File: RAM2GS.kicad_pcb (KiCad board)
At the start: 4 copper layers, 67.1 x 48.5 mm, 54 parts, among them J1 Memory Expansion, J2 JTAG, U1 EPM240T100, U10 74LVC1G04GW, U2 W9864G6KH-6, U3 60M, U4 74AHCT245, U5 74AHC245, U6 74LVT245, U7 74LVT245, U8 LD1117S33, U9 74LVC1G04GW

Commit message: Documentation update
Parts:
- RN2, RN3, RN4, RN5: value 4x47 -> 4x30
- U10, U9: value 74LVC1G04GW -> 74LVC1G04
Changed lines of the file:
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@@
   )
   (page A4)
+  (title_block
+    (title "GW4203D (RAM2GS II)")
+    (date 2020-08-02)
+    (rev 1.0)
+    (company "Garrett's Workshop")
+  )
   (layers
     (0 F.Cu signal)
@@
       (effects (font (size 0.254 0.254) (thickness 0.0635)))
     )
-    (fp_text value 74LVC1G04GW (at 0.35 0 90) (layer F.Fab)
+    (fp_text value 74LVC1G04 (at 0.35 0 90) (layer F.Fab)
       (effects (font (size 0.1905 0.1905) (thickness 0.047625)))
     )
@@
       (effects (font (size 0.254 0.254) (thickness 0.0635)))
     )
-    (fp_text value 74LVC1G04GW (at 0.35 0 90) (layer F.Fab)
+    (fp_text value 74LVC1G04 (at 0.35 0 90) (layer F.Fab)
       (effects (font (size 0.1905 0.1905) (thickness 0.047625)))
     )
@@
       (effects (font (size 0.254 0.254) (thickness 0.0635)))
     )
-    (fp_text value 4x47 (at 0.3 0 90) (layer F.Fab)
+    (fp_text value 4x30 (at 0.3 0 90) (layer F.Fab)
       (effects (font (size 0.1905 0.1905) (thickness 0.047625)))
     )
@@
       (effects (font (size 0.254 0.254) (thickness 0.0635)))
     )
-    (fp_text value 4x47 (at 0.3 0 90) (layer F.Fab)
+    (fp_text value 4x30 (at 0.3 0 90) (layer F.Fab)
       (effects (font (size 0.1905 0.1905) (thickness 0.047625)))
     )
@@
       (effects (font (size 0.254 0.254) (thickness 0.0635)))
     )
-    (fp_text value 4x47 (at 0.3 0) (layer F.Fab)
+    (fp_text value 4x30 (at 0.3 0) (layer F.Fab)
       (effects (font (size 0.1905 0.1905) (thickness 0.047625)))
     )
@@
       (effects (font (size 0.254 0.254) (thickness 0.0635)))
     )
-    (fp_text value 4x47 (at 0.3 0) (layer F.Fab)
+    (fp_text value 4x30 (at 0.3 0) (layer F.Fab)
       (effects (font (size 0.1905 0.1905) (thickness 0.047625)))
     )

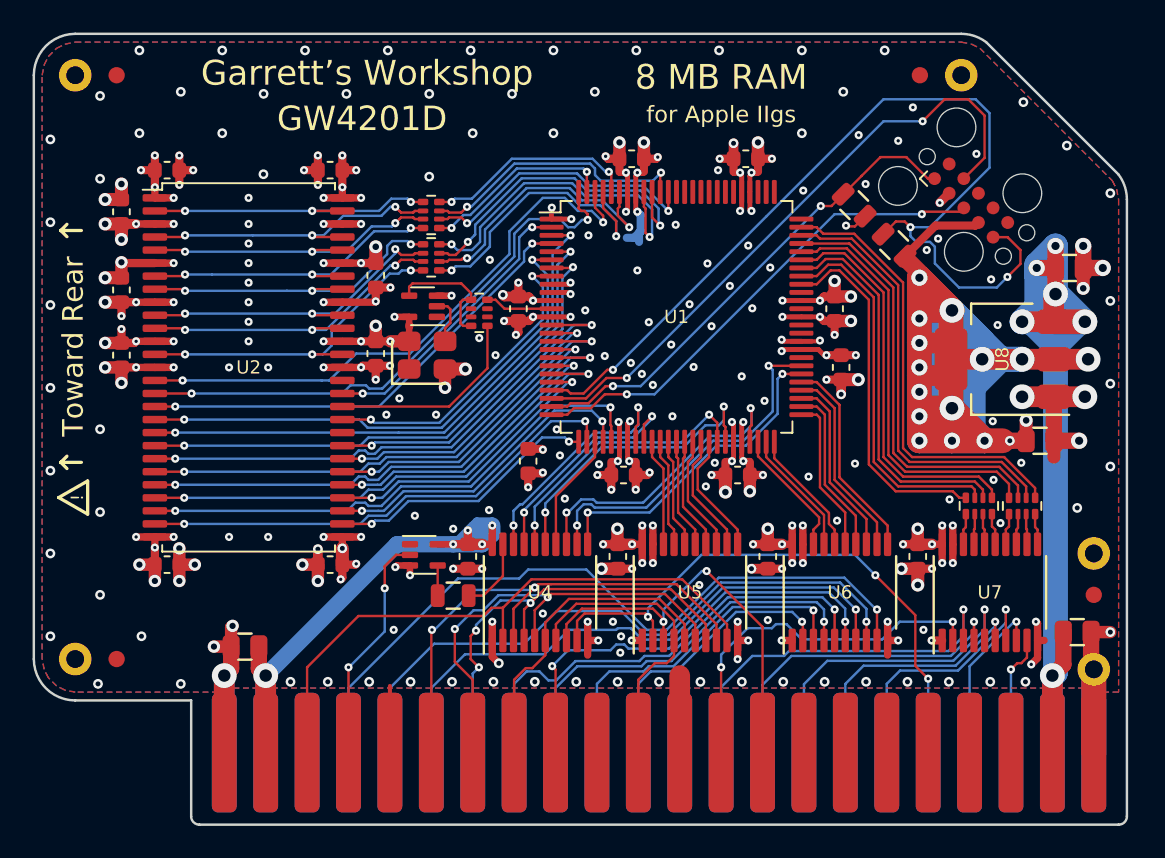
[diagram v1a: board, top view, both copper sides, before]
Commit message: Switch to 7050 oscillator
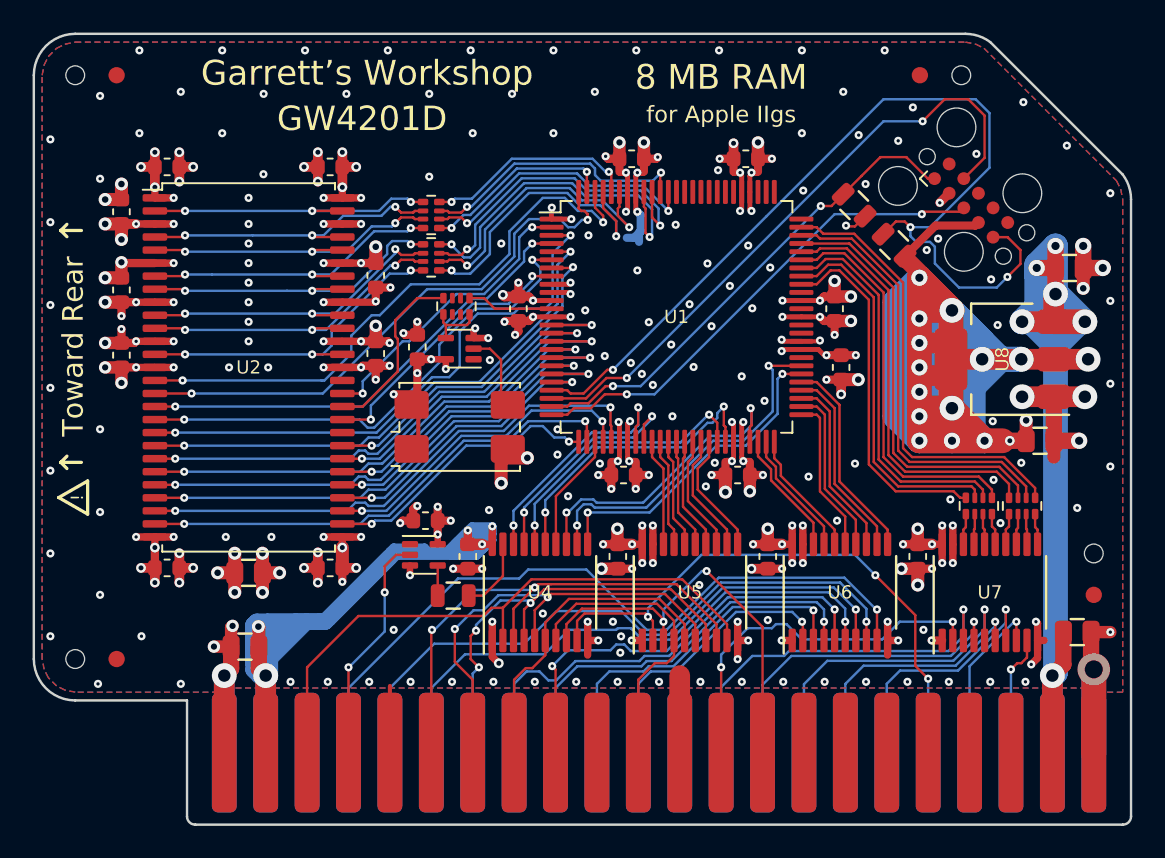
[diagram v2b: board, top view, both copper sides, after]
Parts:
- added C26: 10u, stdpads:C_0805, F.Cu at (59.1, 124.2)
- added C27: 2u2, stdpads:C_0603, F.Cu at (70.0, 121.0)
- H1, H2, H4, H5: footprint stdpads:PasteHole_1.1mm_PTH -> stdpads:PasteHole_1.152mm_NPTH
- R1: value 1k2 -> 22k
- RN1, RN2, RN3, RN4, RN5: value 4x30 -> 4x33
- U3: footprint stdpads:Crystal_SMD_3225-4Pin_3.2x2.5mm -> stdpads:Crystal_SMD_7050-4Pin_7.0x5.0mm
- U5: value 74AHC245 -> 74LVC245
- U6, U7: value 74LVT245 -> 74LVC245
- U8: value LD1117S33 -> AZ1117CH-3.3
- moved C10 9.76 mm to (69.5, 110.4)
- moved U3 4.83 mm to (72.1, 115.3)
- moved U10 3.44 mm to (72.1, 110.5)
- moved RN1 1.46 mm to (71.9, 107.9), turned to 90 degrees
- moved C17 0.20 mm to (54.1, 99.3)
- moved C21 0.20 mm to (54.1, 124.0)
- moved C22 0.20 mm to (64.2, 124.0)
- moved C25 0.20 mm to (64.2, 99.3)
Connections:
- RN1 pad 5: /RClk -> /AClk
- RN1 pad 8: /AClk -> /RClk
- U9 pad 5: +5V -> +3V3
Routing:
- net +5V: track 112.3 -> 172.9 mm
- net +3V3: track 253.5 -> 273.9 mm, vias 99 -> 106
- net GND: track 170.9 -> 177.3 mm
- net Net-(RN1-Pad1): track 7.81 -> 3.52 mm
- net /CKE: track 19.1 -> 17.3 mm
- net /R~RAS~: track 32.4 -> 30.9 mm
- net /RClk: track 12.5 -> 11.0 mm
- net Net-(U10-Pad2): track 3.01 -> 4.18 mm
- net /AClk: track 4.17 -> 5.31 mm
- net /RA11: track 21.9 -> 21.0 mm
- net /BA0: track 33.8 -> 33.0 mm
- net /DQML: track 35.7 -> 36.3 mm
- net /RD4r: track 20.8 -> 21.4 mm
- net /RA4: track 16.8 -> 17.4 mm
- net /RD6r: track 17.5 -> 18.1 mm
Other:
- board size 67.1 x 48.5 mm -> 67.3 x 48.5 mm

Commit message: Fabbed 10/6/2020
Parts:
- RN1, RN2, RN3, RN4, RN5: footprint stdpads:Yageo_YC124 -> stdpads:R4_0402
- U1: value EPM240T100 -> EPM240T100C5N
- U10, U9: value 74LVC1G04 -> 74LVC1G04GW
- U2: value W9864G6KH-6 -> W9812G6KH-6
- U3: footprint stdpads:Crystal_SMD_7050-4Pin_7.0x5.0mm -> stdpads:Crystal_SMD_7050-4Pin_7.0x5.0mm_SiTime
- U4: value 74AHCT245 -> 74AHCT245PW
- U5, U6, U7: value 74LVC245 -> 74LVC245APW
- turned RN1 to 0 degrees
- turned RN2 to 270 degrees
- turned RN3 to 270 degrees
- turned RN4 to 0 degrees
- turned RN5 to 0 degrees
- turned U1 to 270 degrees
- turned U10 to 0 degrees
- turned U4 to 0 degrees
- turned U5 to 0 degrees
- turned U6 to 0 degrees
- turned U7 to 0 degrees
- turned U8 to 0 degrees
- turned U9 to 180 degrees
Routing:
- net GND: vias 247 -> 246
- net +3V3: vias 106 -> 107

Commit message: Fabbed
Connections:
- U2 pad 36: Net-(U2-Pad36) -> GND

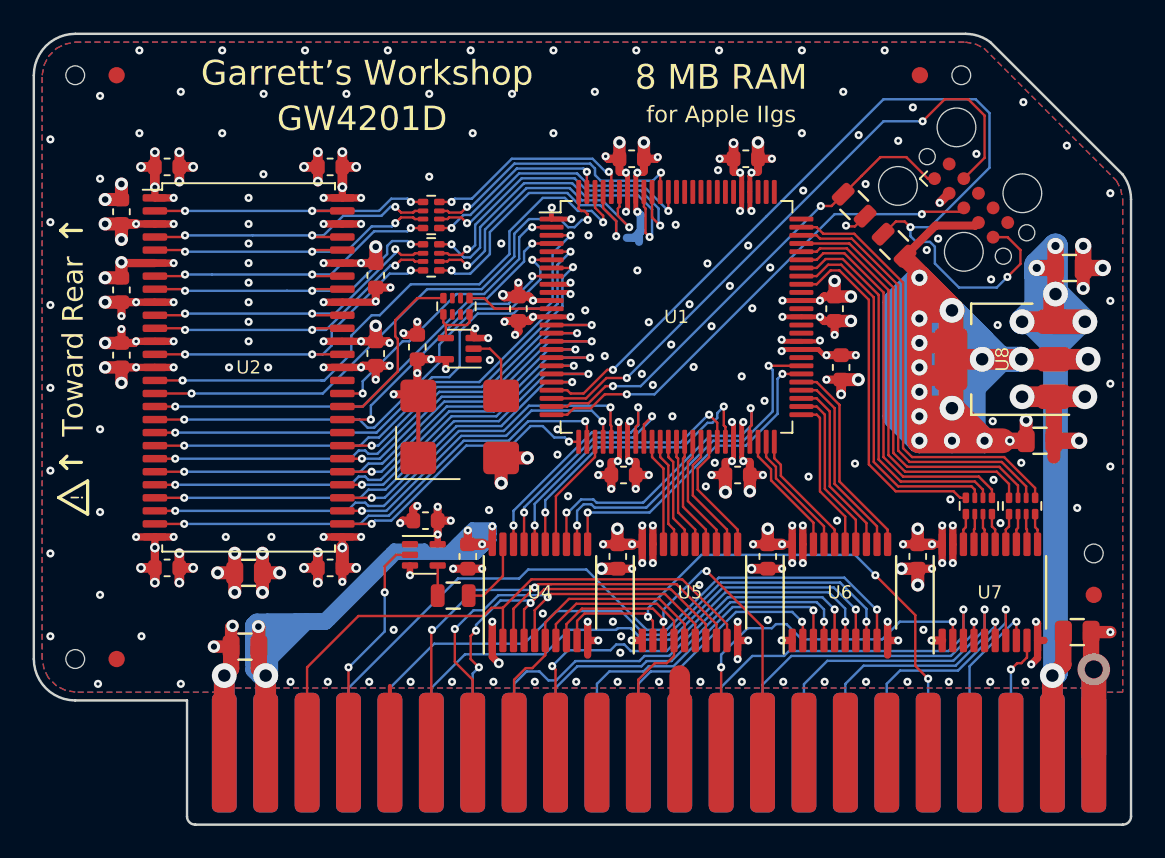
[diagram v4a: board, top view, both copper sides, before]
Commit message: Added 1.8V regulator
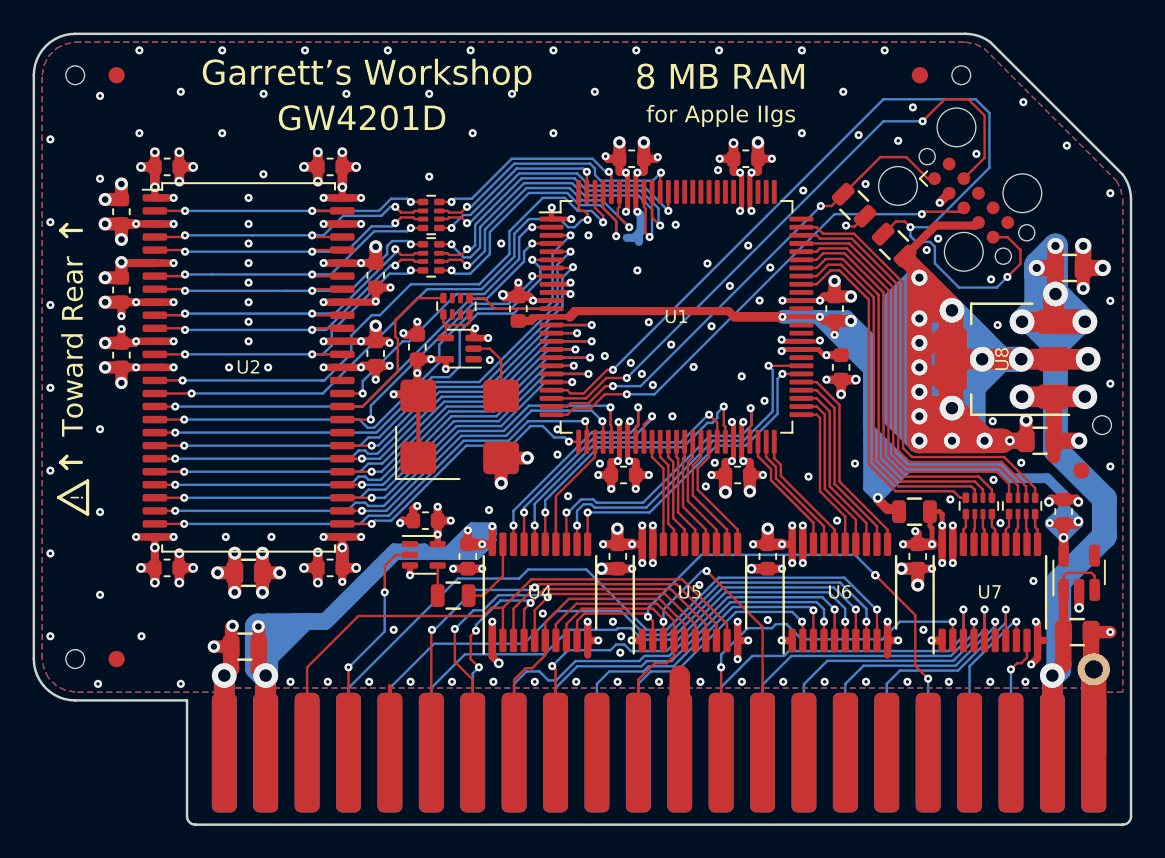
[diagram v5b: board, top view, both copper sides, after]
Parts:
- added C28: 2u2, stdpads:C_0603, F.Cu at (109.2, 120.5)
- added R4: 0, stdpads:R_0805, F.Cu at (100.0, 120.5)
- added U11: DNP, stdpads:SOT-23-5, F.Cu at (110.1, 124.2)
- moved H5 7.89 mm to (111.5, 115.2)
- moved FID3 7.66 mm to (110.2, 118.0)
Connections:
- C14 pad 1: +3V3 -> +1V8
- C9 pad 1: +3V3 -> +1V8
- U1 pad 1: Net-(U1-Pad1) -> GND
- U1 pad 13: +3V3 -> +1V8
- U1 pad 63: +3V3 -> +1V8
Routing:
- net +1V8: track 0.00 -> 143.8 mm, vias 0 -> 8
- net +5V: track 172.9 -> 181.7 mm
- net +3V3: track 273.9 -> 265.5 mm, vias 107 -> 98
- net GND: track 177.3 -> 182.1 mm, vias 246 -> 249
- net Net-(U1-Pad1): track 1.94 -> 0.00 mm, vias 2 -> 0
- net /FD2: vias 3 -> 4
